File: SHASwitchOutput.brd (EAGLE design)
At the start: 47 x 64 mm, 39 parts, among them IC2 HLKPM01, Q1 2N7002, Q2 2N7002, Q3 2N7002, Q4 2N7002

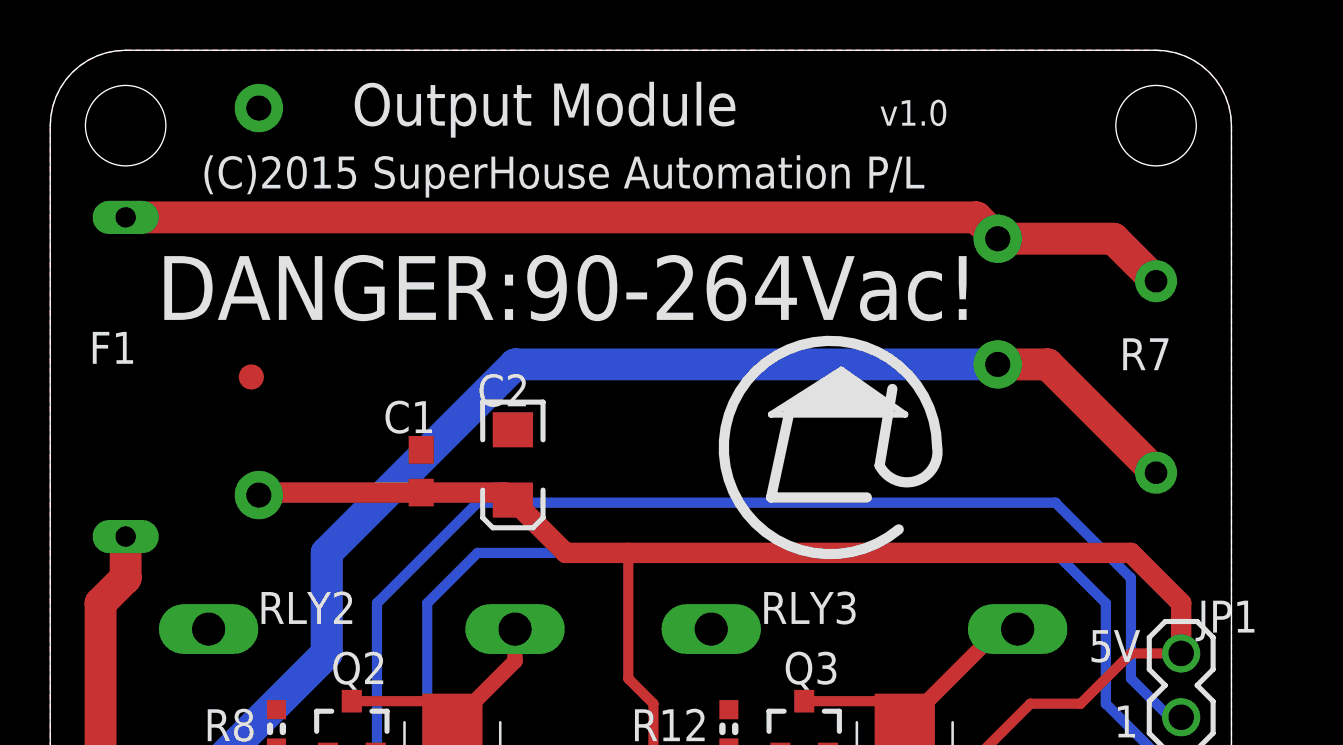
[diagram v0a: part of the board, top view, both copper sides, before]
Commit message: Added GND-Neutral solder jumper (normally open) Changed fuse to vertial orientation
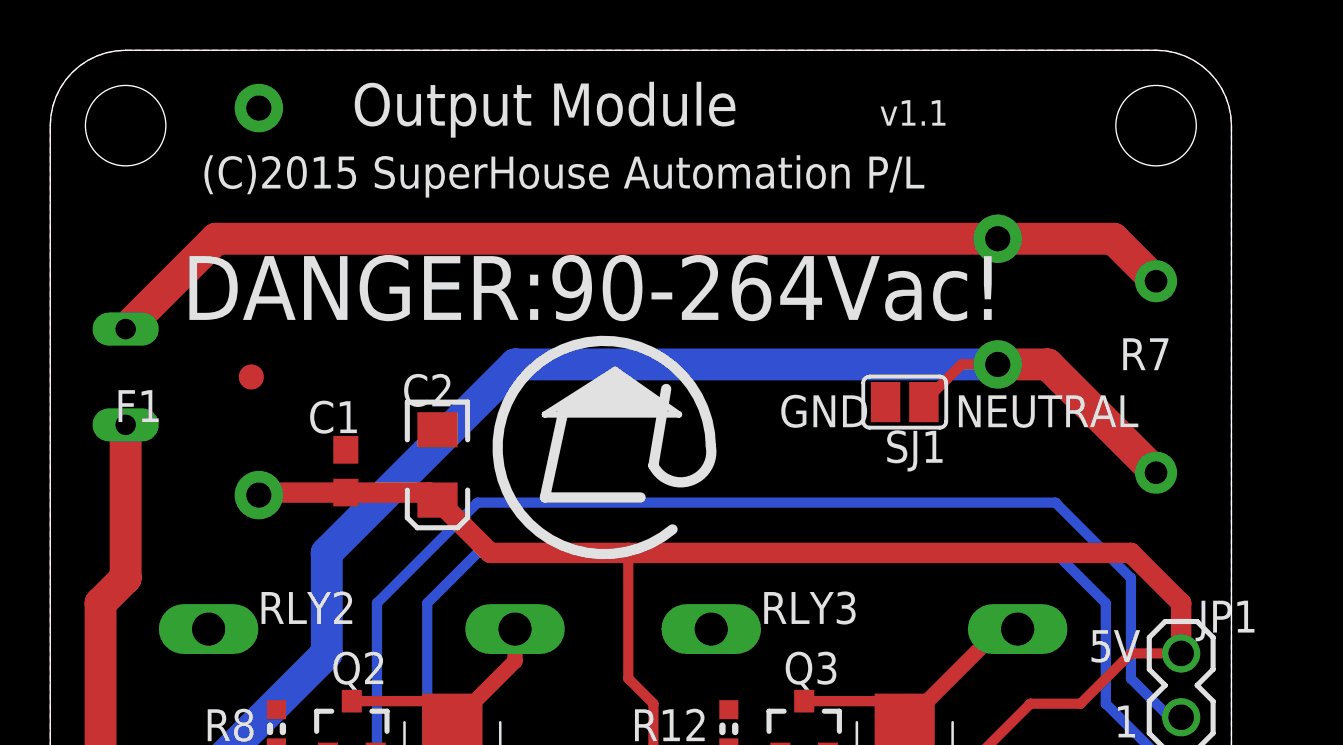
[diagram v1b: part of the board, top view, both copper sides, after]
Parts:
- added SJ1: GND-NEUTRAL-LINK, freetronics-jon:SJ
- F1: device freetronics-jon:PICOFUSE -> freetronics-jon:PICOFUSE-V
- moved C2 3.00 mm to (15.4, 47.5)
- moved C1 3.00 mm to (11.8, 47.2)
- turned F1 to 270 degrees
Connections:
- net $N16: now also F1.1; no longer F1.2
- net ACTIVE: now also F1.2; no longer F1.1
- net GND: now also SJ1.2
- net NEUTRAL: now also SJ1.1
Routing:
- net ACTIVE: track 99.0 -> 103.4 mm
- net NEUTRAL: track 89.1 -> 92.6 mm
- net $N16: track 42.1 -> 43.2 mm
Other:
- board text added: "NEUTRAL"
- board text added: "v1.1"
- board text removed: "v1.0"
